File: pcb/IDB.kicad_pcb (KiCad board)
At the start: 2 copper layers, 77.5 x 50.8 mm, 42 parts, among them J1 Conn_01x10_Socket, J10 Conn_01x03_Socket, J11 Conn_01x03_Socket, J12 Conn_01x03_Socket, J13 Conn_01x03_Socket, J14 Conn_01x03_Socket, J15 Conn_01x03_Socket, J16 Conn_01x03_Socket, J17 Conn_01x03_Socket, J18 Conn_01x03_Socket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

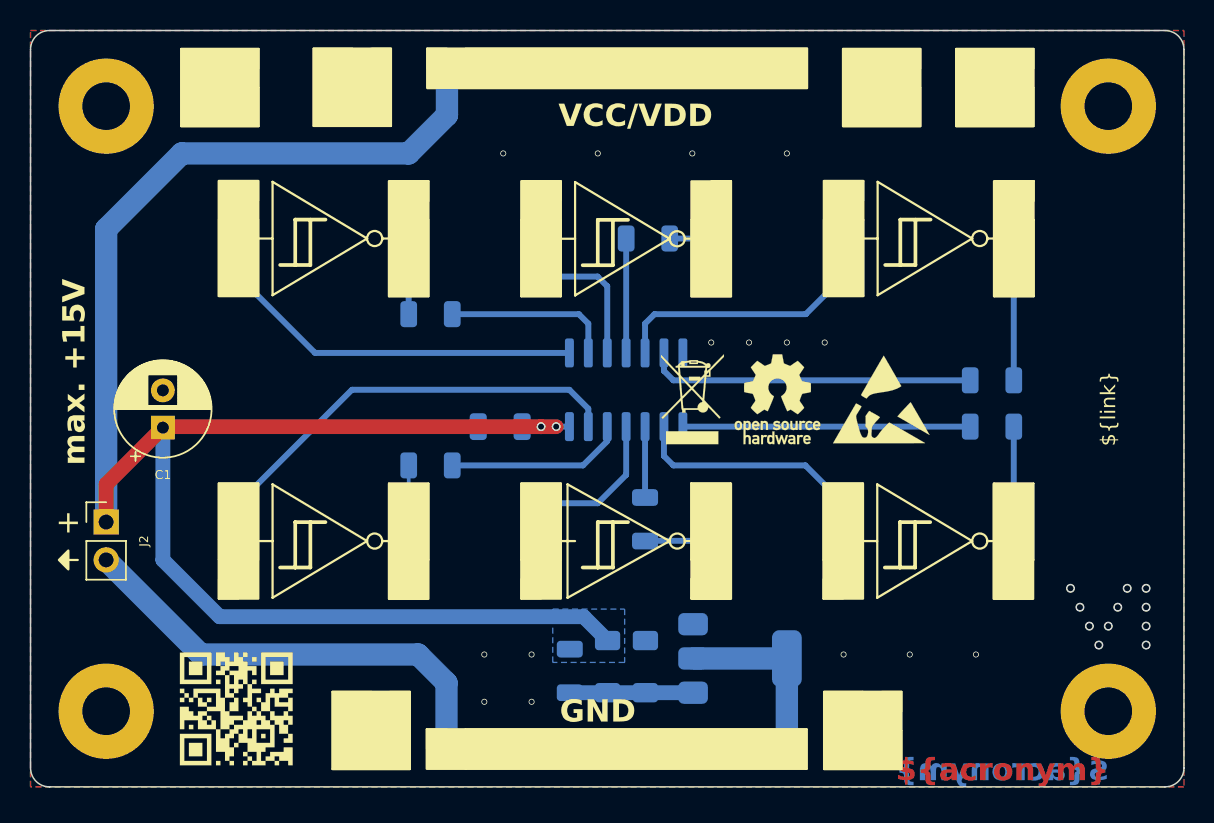
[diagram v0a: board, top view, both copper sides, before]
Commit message: Add push/pull possibility for inputs
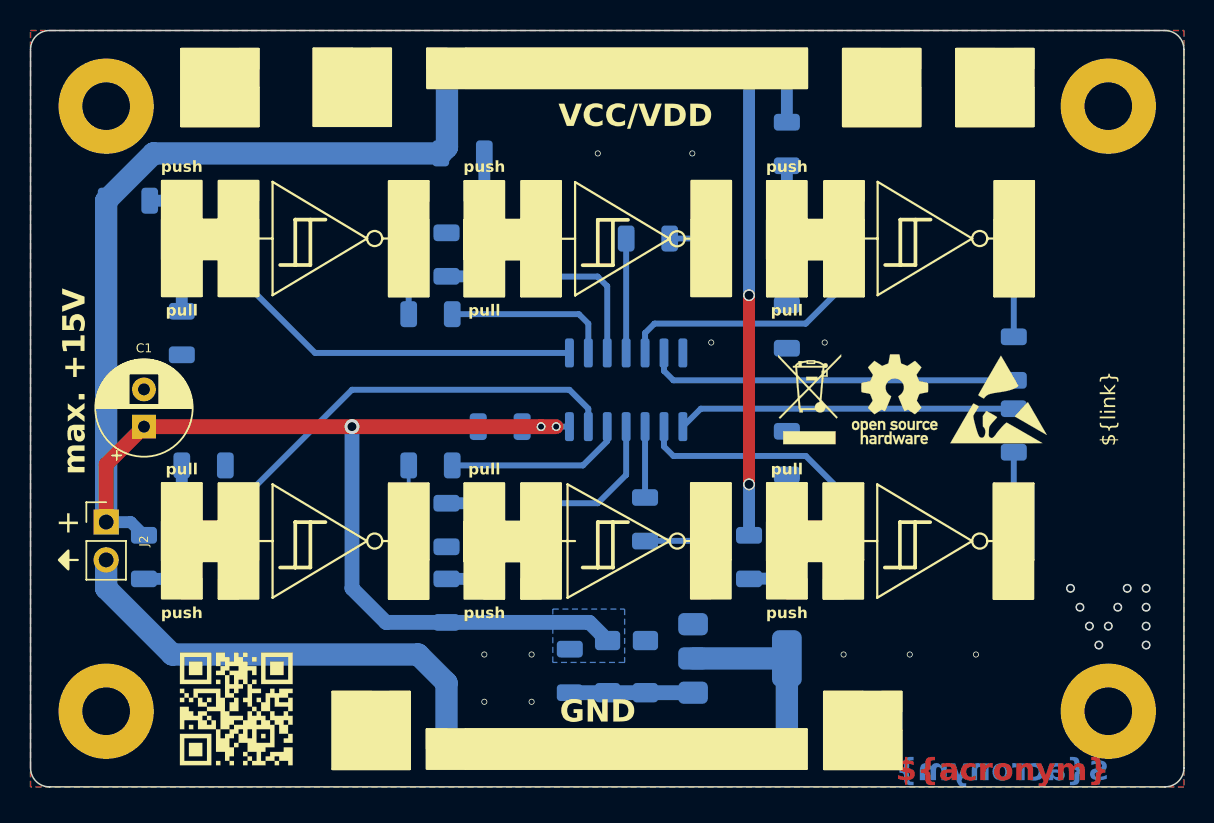
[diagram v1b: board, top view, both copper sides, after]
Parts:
- added J22: Conn_01x03_Pin, Connector_PinHeader_2.54mm:PinHeader_1x03_P2.54mm_Vertical, F.Cu at (129.5, 113.0)
- added J23: Conn_01x03_Pin, Connector_PinHeader_2.54mm:PinHeader_1x03_P2.54mm_Vertical, F.Cu at (149.9, 113.0)
- added J24: Conn_01x03_Pin, Connector_PinHeader_2.54mm:PinHeader_1x03_P2.54mm_Vertical, F.Cu at (170.2, 113.0)
- added J25: Conn_01x03_Pin, Connector_PinHeader_2.54mm:PinHeader_1x03_P2.54mm_Vertical, F.Cu at (170.2, 87.6)
- added J26: Conn_01x03_Pin, Connector_PinHeader_2.54mm:PinHeader_1x03_P2.54mm_Vertical, F.Cu at (149.9, 87.6)
- added J27: Conn_01x03_Pin, Connector_PinHeader_2.54mm:PinHeader_1x03_P2.54mm_Vertical, F.Cu at (129.5, 87.6)
- added R10: 10k, Resistor_SMD:R_1206_3216Metric, B.Cu at (147.3, 114.5)
- added R11: 10k, Resistor_SMD:R_1206_3216Metric, B.Cu at (147.3, 109.4)
- added R12: 10k, Resistor_SMD:R_1206_3216Metric, B.Cu at (167.6, 111.6)
- added R13: 10k, Resistor_SMD:R_1206_3216Metric, B.Cu at (170.2, 104.6)
- added R14: 10k, Resistor_SMD:R_1206_3216Metric, B.Cu at (170.2, 83.8)
- added R15: 10k, Resistor_SMD:R_1206_3216Metric, B.Cu at (170.2, 96.1)
- added R16: 10k, Resistor_SMD:R_1206_3216Metric, B.Cu at (148.4, 84.5)
- added R17: 10k, Resistor_SMD:R_1206_3216Metric, B.Cu at (147.3, 91.2)
- added R18: 10k, Resistor_SMD:R_1206_3216Metric, B.Cu at (125.9, 87.6)
- added R19: 10k, Resistor_SMD:R_1206_3216Metric, B.Cu at (129.5, 96.5)
- added R8: 10k, Resistor_SMD:R_1206_3216Metric, B.Cu at (127.0, 111.6)
- added R9: 10k, Resistor_SMD:R_1206_3216Metric, B.Cu at (131.0, 105.4)
- moved FID3 7.87 mm to (177.4, 101.0)
- moved FID1 7.87 mm to (184.4, 101.0)
- moved FID2 7.87 mm to (171.7, 101.0)
- moved R4 2.07 mm to (185.4, 98.2), turned to 90 degrees
- moved R3 1.48 mm to (185.4, 103.1), turned to -90 degrees
- moved C1 1.27 mm to (127.0, 102.8)
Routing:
- net VCC: track 127.4 -> 157.0 mm, vias 2 -> 5
- net Net-(J13-Pin_1): track 21.7 -> 25.5 mm
- net Net-(J12-Pin_1): track 20.4 -> 24.2 mm
- net Net-(J10-Pin_1): track 33.5 -> 37.3 mm
- net Net-(J15-Pin_1): track 29.4 -> 33.2 mm
- net Net-(J14-Pin_1): track 14.3 -> 18.1 mm
- net Net-(J11-Pin_1): track 14.8 -> 18.6 mm
- net Net-(R3-Pad1): track 19.3 -> 22.7 mm
- net Net-(J26-Pin_1): track 0.00 -> 3.19 mm
- net Net-(J19-Pin_1): track 12.1 -> 9.14 mm
- net Net-(R4-Pad1): track 22.0 -> 25.0 mm
- net Net-(J26-Pin_3): track 0.00 -> 2.55 mm
- net Net-(J24-Pin_1): track 0.00 -> 2.55 mm
- net Net-(J22-Pin_1): track 0.00 -> 2.55 mm
- net Net-(J23-Pin_3): track 0.00 -> 2.54 mm
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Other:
- board text added: "pull"
- board text added: "push"

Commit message: Optimize silkscreen
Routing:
- net Net-(J2-Pin_2): track 44.3 -> 43.8 mm
- net GND: vias 22 -> 36
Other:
- board text added: "Down"
- board text added: "Pull"
- board text added: "Up"
- board text removed: "pull"
- board text removed: "push"
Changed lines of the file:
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@@
 		(tags "Through hole pin header THT 1x02 2.54mm single row")
 		(property "Reference" "J2"
-			(at 2.54 1.275 90)
+			(at 0.02 4.685 90)
 			(layer "F.SilkS")
 			(effects
@@
 	)
 	(gr_rect
-		(start 128.21 86.3)
+		(start 128.16 86.25)
 		(end 130.87 94.04)
 		(stroke
@@
 	)
 	(gr_rect
-		(start 128.21 88.9)
-		(end 134.62 91.56)
+		(start 128.16 106.555)
+		(end 130.92 114.395)
 		(stroke
 			(width 0.15)
@@
 	)
 	(gr_rect
-		(start 128.21 106.605)
-		(end 130.87 114.345)
+		(start 128.21 88.9)
+		(end 134.62 91.56)
 		(stroke
 			(width 0.15)
@@
 	)
 	(gr_rect
-		(start 148.53 86.315)
+		(start 148.48 86.265)
 		(end 151.19 94.055)
 		(stroke
@@
 	)
 	(gr_rect
-		(start 148.53 88.915)
-		(end 154.94 91.575)
+		(start 148.48 106.57)
+		(end 151.24 114.41)
 		(stroke
 			(width 0.15)
@@
 	)
 	(gr_rect
-		(start 148.53 106.62)
-		(end 151.19 114.36)
+		(start 148.53 88.915)
+		(end 154.94 91.575)
 		(stroke
 			(width 0.15)
@@
 	)
 	(gr_rect
-		(start 168.85 86.315)
+		(start 168.8 86.265)
 		(end 171.51 94.055)
 		(stroke
@@
 	)
 	(gr_rect
-		(start 168.85 88.915)
-		(end 175.26 91.575)
+		(start 168.8 106.555)
+		(end 171.56 114.395)
 		(stroke
 			(width 0.15)
@@
 	)
 	(gr_rect
-		(start 168.85 106.605)
-		(end 171.51 114.345)
+		(start 168.85 88.915)
+		(end 175.26 91.575)
 		(stroke
 			(width 0.15)
@@
 		)
 	)
-	(gr_text "push"
+	(gr_text "Up"
 		(at 129.54 85.344 0)
 		(layer "F.SilkS")
@@
 		)
 	)
-	(gr_text "pull"
+	(gr_text "Down"
 		(at 129.54 94.996 0)
 		(layer "F.SilkS")
@@
 		)
 	)
-	(gr_text "pull"
+	(gr_text "Down"
 		(at 129.54 105.664 0)
 		(layer "F.SilkS")
@@
 		)
 	)
-	(gr_text "push"
+	(gr_text "Up"
 		(at 129.54 115.316 0)
 		(layer "F.SilkS")
@@
 		)
 	)
-	(gr_text "push"
+	(gr_text "Up"
 		(at 149.86 85.344 0)
 		(layer "F.SilkS")
@@
 		)
 	)
-	(gr_text "pull"
+	(gr_text "Down"
 		(at 149.86 94.996 0)
 		(layer "F.SilkS")
@@
 		)
 	)
-	(gr_text "pull"
+	(gr_text "Down"
 		(at 149.86 105.664 0)
 		(layer "F.SilkS")
@@
 		)
 	)
-	(gr_text "push"
+	(gr_text "Up"
 		(at 149.86 115.316 0)
 		(layer "F.SilkS")
@@
 		)
 	)
-	(gr_text "push"
+	(gr_text "Up"
 		(at 170.18 85.344 0)
 		(layer "F.SilkS")
@@
 		)
 	)
-	(gr_text "pull"
+	(gr_text "Down"
 		(at 170.18 94.996 0)
 		(layer "F.SilkS")
@@
 		)
 	)
-	(gr_text "pull"
+	(gr_text "Down"
 		(at 170.18 105.664 0)
 		(layer "F.SilkS")
@@
 		)
 	)
-	(gr_text "push"
+	(gr_text "Up"
 		(at 170.18 115.316 0)
 		(layer "F.SilkS")
@@
 		)
 	)
+	(gr_text "Pull"
+		(at 127.63 90.2 90)
+		(layer "F.SilkS")
+		(effects
+			(font
+				(size 0.75 0.75)
+				(thickness 0.12)
+				(bold yes)
+			)
+		)
+	)
+	(gr_text "Pull"
+		(at 127.63 110.45 90)
+		(layer "F.SilkS")
+		(effects
+			(font
+				(size 0.75 0.75)
+				(thickness 0.12)
+				(bold yes)
+			)
+		)
+	)
+	(gr_text "Pull"
+		(at 147.88 90.2 90)
+		(layer "F.SilkS")
+		(effects
+			(font
+				(size 0.75 0.75)
+				(thickness 0.12)
+				(bold yes)
+			)
+		)
+	)
+	(gr_text "Pull"
+		(at 147.88 110.45 90)
+		(layer "F.SilkS")
+		(effects
+			(font
+				(size 0.75 0.75)
+				(thickness 0.12)
+				(bold yes)
+			)
+		)
+	)
+	(gr_text "Pull"
+		(at 168.13 90.2 90)
+		(layer "F.SilkS")
+		(effects
+			(font
+				(size 0.75 0.75)
+				(thickness 0.12)
+				(bold yes)
+			)
+		)
+	)
+	(gr_text "Pull"
+		(at 168.13 110.45 90)
+		(layer "F.SilkS")
+		(effects
+			(font
+				(size 0.75 0.75)
+				(thickness 0.12)
+				(bold yes)
+			)
+		)
+	)
 	(gr_text "${link}"
 		(at 191.77 101.6 90)
@@
 	)
 	(via
+		(at 166.38 97.2)
+		(size 0.4)
+		(drill 0.3)
+		(layers "F.Cu" "B.Cu")
+		(free yes)
+		(net 1)
+	)
+	(via
 		(at 194.31 116.205)
 		(size 0.6)
@@
 	)
 	(via
+		(at 146.13 99.2)
+		(size 0.4)
+		(drill 0.3)
+		(layers "F.Cu" "B.Cu")
+		(free yes)
+		(net 1)
+	)
+	(via
 		(at 194.31 114.935)
 		(size 0.6)
@@
 	)
 	(via
+		(at 131.88 116.95)
+		(size 0.4)
+		(drill 0.3)
+		(layers "F.Cu" "B.Cu")
+		(free yes)
+		(net 1)
+	)
+	(via
+		(at 142.63 101.45)
+		(size 0.4)
+		(drill 0.3)
+		(layers "F.Cu" "B.Cu")
+		(free yes)
+		(net 1)
+	)
+	(via
+		(at 166.38 103.45)
+		(size 0.4)
+		(drill 0.3)
+		(layers "F.Cu" "B.Cu")
+		(free yes)
+		(net 1)
+	)
+	(via
 		(at 189.865 114.935)
 		(size 0.6)
@@
 	)
 	(via
+		(at 149.63 99.2)
+		(size 0.4)
+		(drill 0.3)
+		(layers "F.Cu" "B.Cu")
+		(free yes)
+		(net 1)
+	)
+	(via
 		(at 149.86 118.11)
 		(size 0.4)
@@
 	)
 	(via
+		(at 139.13 96.7)
+		(size 0.4)
+		(drill 0.3)
+		(layers "F.Cu" "B.Cu")
+		(free yes)
+		(net 1)
+	)
+	(via
 		(at 190.5 116.205)
 		(size 0.6)
@@
 	)
 	(via
+		(at 141.88 116.95)
+		(size 0.4)
+		(drill 0.3)
+		(layers "F.Cu" "B.Cu")
+		(free yes)
+		(net 1)
+	)
+	(via
 		(at 178.435 118.11)
 		(size 0.4)
@@
 	)
 	(via
+		(at 142.63 99.2)
+		(size 0.4)
+		(drill 0.3)
+		(layers "F.Cu" "B.Cu")
+		(free yes)
+		(net 1)
+	)
+	(via
+		(at 174.13 103.45)
+		(size 0.4)
+		(drill 0.3)
+		(layers "F.Cu" "B.Cu")
+		(free yes)
+		(net 1)
+	)
+	(via
 		(at 157.48 84.455)
 		(size 0.4)
@@
 	)
 	(via
-		(at 172.72 97.155)
+		(at 174.13 97.155)
+		(size 0.4)
+		(drill 0.3)
+		(layers "F.Cu" "B.Cu")
+		(free yes)
+		(net 1)
+	)
+	(via
+		(at 142.63 96.7)
 		(size 0.4)
 		(drill 0.3)
@@
 	)
 	(via
+		(at 165.13 103.45)
+		(size 0.4)
+		(drill 0.3)
+		(layers "F.Cu" "B.Cu")
+		(free yes)
+		(net 1)
+	)
+	(via
 		(at 149.86 121.285)
 		(size 0.4)
@@
 	)
 	(via
+		(at 136.88 116.95)
+		(size 0.4)
+		(drill 0.3)
+		(layers "F.Cu" "B.Cu")
+		(free yes)
+		(net 1)
+	)
+	(via
 		(at 189.23 113.665)
 		(size 0.6)
@@
 	)
 	(via
+		(at 146.13 101.45)
+		(size 0.4)
+		(drill 0.3)
+		(layers "F.Cu" "B.Cu")
+		(free yes)
+		(net 1)
+	)
+	(via
 		(at 193.04 113.665)
 		(size 0.6)
@@
 	)
 	(segment
-		(start 147.32 120.015)
-		(end 147.32 124.46)
+		(start 124.46 113.665)
+		(end 129.495 118.7)
 		(width 1.5)
 		(layer "B.Cu")
@@
 	)
 	(segment
-		(start 162.535 124.435)
-		(end 162.56 124.46)
+		(start 129.495 118.7)
+		(end 145.13 118.7)
 		(width 1.5)
 		(layer "B.Cu")
@@
 	)
 	(segment
-		(start 128.905 118.11)
-		(end 145.415 118.11)
+		(start 162.535 124.435)
+		(end 162.56 124.46)
 		(width 1.5)
 		(layer "B.Cu")
@@
 	)
 	(segment
-		(start 124.46 113.665)
-		(end 128.905 118.11)
+		(start 147.32 120.89)
+		(end 147.32 124.46)
 		(width 1.5)
 		(layer "B.Cu")
@@
 	)
 	(segment
-		(start 124.46 111.755)
-		(end 124.46 113.665)
+		(start 145.13 118.7)
+		(end 147.32 120.89)
 		(width 1.5)
 		(layer "B.Cu")
@@
 	)
 	(segment
-		(start 145.415 118.11)
-		(end 147.32 120.015)
+		(start 163.88 118.375)
+		(end 170.18 118.375)
 		(width 1.5)
 		(layer "B.Cu")
@@
 	)
 	(segment
-		(start 163.88 118.375)
-		(end 170.18 118.375)
+		(start 124.46 111.755)
+		(end 124.46 113.665)
 		(width 1.5)
 		(layer "B.Cu")
